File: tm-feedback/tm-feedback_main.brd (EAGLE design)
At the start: 60.1 x 40.3 mm, 45 parts

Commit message: Changed LEDs to more accurate values
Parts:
- BT:LED1: value BLUE -> YELLOW
- BT:LED2: value GREEN -> RED
- BT:LED3, UC:LED2: value RED -> GREEN
- BT:R1, BT:R3, BT:R4, UC:R6: value 60Ω -> 53.6Ω
- PS:R1: value 60 -> 53.6Ω
- UC:R3: value 69Ω -> 53.6Ω
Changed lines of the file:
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@@
 <attribute name="VALUE" x="9.98" y="36.562" size="1.27" layer="27" rot="R90"/>
 </element>
-<element name="PS:R1" library="resistor" package="R0805" value="60" x="9.5212" y="37.8028" smashed="yes" rot="R90">
+<element name="PS:R1" library="resistor" package="R0805" value="53.6Ω" x="9.5212" y="37.8028" smashed="yes" rot="R90">
 <attribute name="NAME" x="8.2512" y="37.1678" size="1.27" layer="25" rot="R90"/>
 <attribute name="VALUE" x="12.0612" y="37.1678" size="1.27" layer="27" rot="R90"/>
@@
 <attribute name="VALUE" x="45.3162" y="30.9624" size="1.27" layer="27" rot="R270"/>
 </element>
-<element name="BT:R3" library="resistor" package="R0805" value="60Ω" x="40.312" y="22.93" smashed="yes">
+<element name="BT:R3" library="resistor" package="R0805" value="53.6Ω" x="40.312" y="22.93" smashed="yes">
 <attribute name="NAME" x="39.677" y="24.2" size="1.27" layer="25"/>
 <attribute name="VALUE" x="39.677" y="20.39" size="1.27" layer="27"/>
 </element>
-<element name="BT:LED2" library="led" package="CHIPLED_0805" value="GREEN" x="40.258" y="24.712" smashed="yes" rot="R270">
+<element name="BT:LED2" library="led" package="CHIPLED_0805" value="RED" x="40.258" y="24.712" smashed="yes" rot="R270">
 <attribute name="NAME" x="38.988" y="25.982" size="1.27" layer="25"/>
 <attribute name="VALUE" x="38.988" y="22.172" size="1.27" layer="27"/>
 </element>
-<element name="BT:R4" library="resistor" package="R0805" value="60Ω" x="40.272" y="20.532" smashed="yes">
+<element name="BT:R4" library="resistor" package="R0805" value="53.6Ω" x="40.272" y="20.532" smashed="yes">
 <attribute name="NAME" x="39.637" y="21.802" size="1.27" layer="25"/>
 <attribute name="VALUE" x="39.637" y="17.992" size="1.27" layer="27"/>
 </element>
-<element name="BT:LED3" library="led" package="CHIPLED_0805" value="RED" x="40.288" y="18.722" smashed="yes" rot="R270">
+<element name="BT:LED3" library="led" package="CHIPLED_0805" value="GREEN" x="40.288" y="18.722" smashed="yes" rot="R270">
 <attribute name="NAME" x="39.018" y="19.992" size="1.27" layer="25"/>
 <attribute name="VALUE" x="39.018" y="16.182" size="1.27" layer="27"/>
 </element>
-<element name="BT:R1" library="resistor" package="R0805" value="60Ω" x="40.368" y="16.722" smashed="yes">
+<element name="BT:R1" library="resistor" package="R0805" value="53.6Ω" x="40.368" y="16.722" smashed="yes">
 <attribute name="NAME" x="39.733" y="17.992" size="1.27" layer="25"/>
 <attribute name="VALUE" x="39.733" y="14.182" size="1.27" layer="27"/>
 </element>
-<element name="BT:LED1" library="led" package="CHIPLED_0805" value="BLUE" x="40.384" y="14.658" smashed="yes" rot="R270">
+<element name="BT:LED1" library="led" package="CHIPLED_0805" value="YELLOW" x="40.384" y="14.658" smashed="yes" rot="R270">
 <attribute name="NAME" x="39.114" y="15.928" size="1.27" layer="25"/>
 <attribute name="VALUE" x="39.114" y="12.118" size="1.27" layer="27"/>
@@
 <attribute name="VALUE" x="30.102" y="9.042" size="1.27" layer="27" rot="R180"/>
 </element>
-<element name="UC:LED2" library="led" package="CHIPLED_0805" value="RED" x="33.49" y="28.78" smashed="yes" rot="R180">
+<element name="UC:LED2" library="led" package="CHIPLED_0805" value="GREEN" x="33.49" y="28.78" smashed="yes" rot="R180">
 <attribute name="NAME" x="34.76" y="30.05" size="1.27" layer="25" rot="R270"/>
 <attribute name="VALUE" x="30.95" y="30.05" size="1.27" layer="27" rot="R270"/>
 </element>
-<element name="UC:R3" library="resistor" package="R0805" value="69Ω" x="31.558" y="28.834" smashed="yes" rot="R270">
+<element name="UC:R3" library="resistor" package="R0805" value="53.6Ω" x="31.558" y="28.834" smashed="yes" rot="R270">
 <attribute name="NAME" x="32.828" y="29.469" size="1.27" layer="25" rot="R270"/>
 <attribute name="VALUE" x="29.018" y="29.469" size="1.27" layer="27" rot="R270"/>
@@
 <attribute name="VALUE" x="50.88" y="4.612" size="1.27" layer="27" rot="R180"/>
 </element>
-<element name="UC:R6" library="resistor" package="R0805" value="60Ω" x="49.61" y="4.326" smashed="yes" rot="R180">
+<element name="UC:R6" library="resistor" package="R0805" value="53.6Ω" x="49.61" y="4.326" smashed="yes" rot="R180">
 <attribute name="NAME" x="50.245" y="3.056" size="1.27" layer="25" rot="R180"/>
 <attribute name="VALUE" x="50.245" y="6.866" size="1.27" layer="27" rot="R180"/>

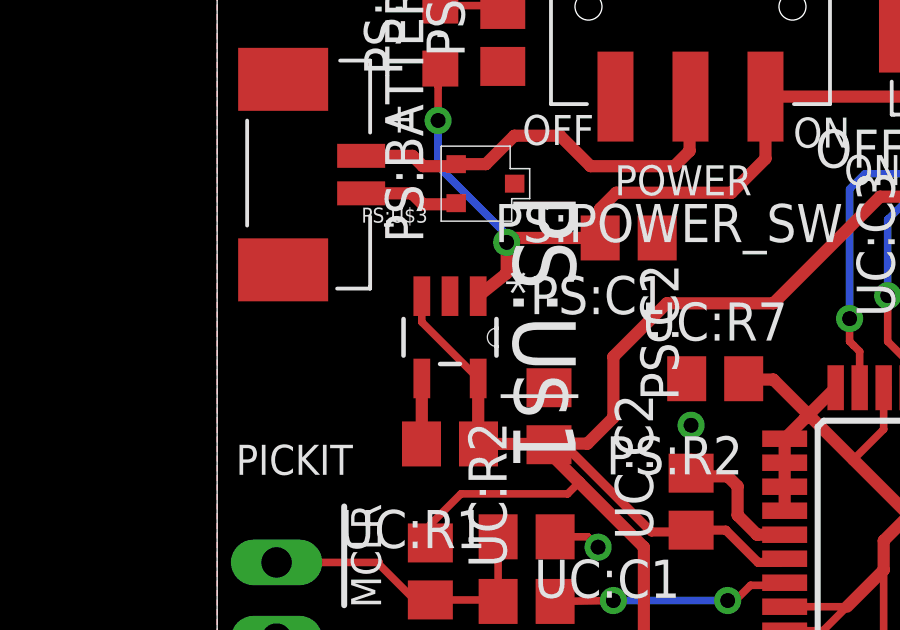
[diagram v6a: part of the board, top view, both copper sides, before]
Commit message: Fix power supply, shutdown should be connected to Vin not Vout
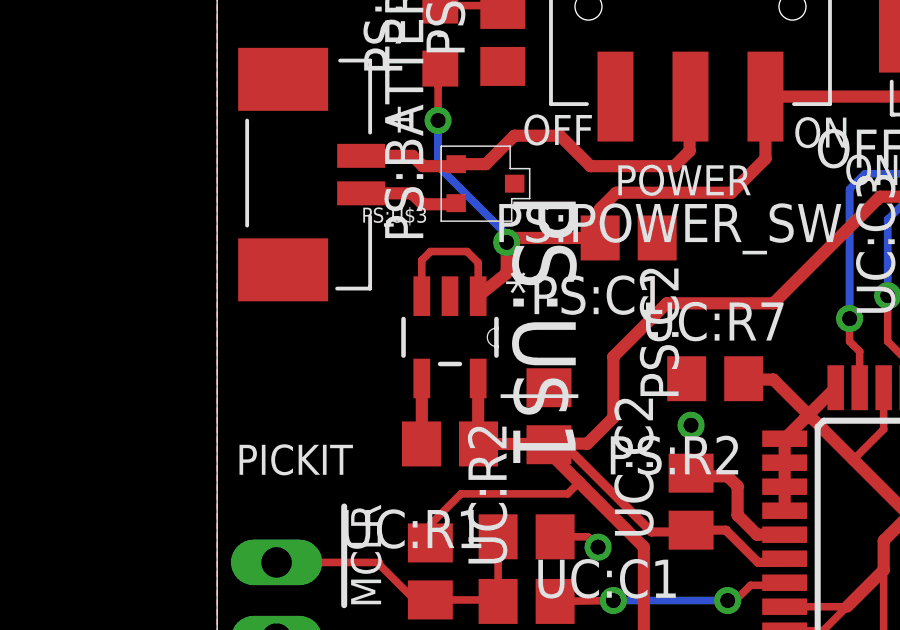
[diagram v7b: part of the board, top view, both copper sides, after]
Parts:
- PS:C1, PS:C2: value (none) -> 10uF
- PS:R2: value 60 -> 10k
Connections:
- net +3V3: no longer PS:U$1.3
- net N$5: now also PS:U$1.3
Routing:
- net N$5: track 29.7 -> 34.1 mm
- net +3V3: track 151.7 -> 148.2 mm
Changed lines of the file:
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@@
 <setting verticaltext="up"/>
 </settings>
-<grid distance="1" unitdist="mm" unit="mm" style="lines" multiple="10" display="yes" altdistance="0.01" altunitdist="mm" altunit="mm"/>
+<grid distance="8" unitdist="mil" unit="mil" style="lines" multiple="10" display="yes" altdistance="0.01" altunitdist="mm" altunit="mm"/>
 <layers>
 <layer number="1" name="Top" color="4" fill="1" visible="yes" active="yes"/>
@@
 <attribute name="VALUE" x="7.018" y="32.996" size="0.5" layer="27" rot="R180"/>
 </element>
-<element name="PS:C1" library="rcl" package="C0805" value="" x="13.718" y="31.136" smashed="yes" rot="R180">
+<element name="PS:C1" library="rcl" package="C0805" value="10uF" x="13.718" y="31.136" smashed="yes" rot="R180">
 <attribute name="NAME" x="14.988" y="29.866" size="1.27" layer="25" rot="R180"/>
 <attribute name="VALUE" x="14.988" y="33.676" size="1.27" layer="27" rot="R180"/>
 </element>
-<element name="PS:C2" library="rcl" package="C0805" value="" x="11.062" y="25.194" smashed="yes" rot="R270">
+<element name="PS:C2" library="rcl" package="C0805" value="10uF" x="11.062" y="25.194" smashed="yes" rot="R270">
 <attribute name="NAME" x="14.11" y="30.274" size="1.27" layer="25" rot="R270"/>
 <attribute name="VALUE" x="8.522" y="26.464" size="1.27" layer="27" rot="R270"/>
 </element>
-<element name="PS:R2" library="resistor" package="R0805" value="60" x="7.762" y="24.27" smashed="yes">
+<element name="PS:R2" library="resistor" package="R0805" value="10k" x="7.762" y="24.27" smashed="yes">
 <attribute name="NAME" x="12.969" y="23.254" size="1.27" layer="25"/>
 <attribute name="VALUE" x="7.127" y="21.73" size="1.27" layer="27"/>
@@
 <contactref element="BTN:U1" pad="5"/>
 <contactref element="PS:R2" pad="2"/>
-<contactref element="PS:U$1" pad="3"/>
 <contactref element="PS:C2" pad="2"/>
 <contactref element="PS:U$1" pad="5"/>
@@
 <wire x1="54.9884" y1="9.645" x2="54.9884" y2="12.822" width="0.254" layer="1"/>
 <wire x1="54.9884" y1="12.822" x2="55.17" y2="13.0036" width="0.254" layer="1"/>
-<wire x1="6.8222" y1="29.1956" x2="6.8222" y2="28.332" width="0.254" layer="1"/>
-<wire x1="6.8222" y1="28.332" x2="8.7018" y2="26.4524" width="0.254" layer="1"/>
 <wire x1="15.8" y1="21.396" x2="16.958" y2="21.396" width="0.3048" layer="1"/>
 <wire x1="16.958" y1="21.396" x2="18.034" y2="20.32" width="0.3048" layer="1"/>
@@
 <wire x1="12.766040625" y1="32.11068125" x2="12.766040625" y2="31.137959375" width="0.4064" layer="1"/>
 <wire x1="12.766040625" y1="31.137959375" x2="12.768" y2="31.136" width="0.4064" layer="1"/>
+<contactref element="PS:U$1" pad="3"/>
+<wire x1="6.8222" y1="29.1956" x2="6.8222" y2="30.3934" width="0.254" layer="1"/>
+<wire x1="6.8222" y1="30.3934" x2="7.112" y2="30.6832" width="0.254" layer="1"/>
+<wire x1="7.112" y1="30.6832" x2="8.3312" y2="30.6832" width="0.254" layer="1"/>
+<wire x1="8.3312" y1="30.6832" x2="8.7018" y2="30.3126" width="0.254" layer="1"/>
+<wire x1="8.7018" y1="30.3126" x2="8.7018" y2="29.1956" width="0.254" layer="1"/>
 </signal>
 </signals>
